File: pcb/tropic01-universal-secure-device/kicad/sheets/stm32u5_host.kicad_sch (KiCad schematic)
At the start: 1 part, among them U1 STM32U585VIT6

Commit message: feat: materialize tropic01 schematic bindings
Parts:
- U1: MountProfile Core -> (none)
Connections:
- new net: U1.10 (VSS), U1.27 (VSS), U1.49 (VSS), U1.74 (VSS), U1.99 (VSS)
- new net BOOT0: U1.62 (PD15)
- new net BTN_LEFT: U1.58 (PD11)
- new net BTN_RIGHT: U1.57 (PD10)
- new net EXP_UART_RX: U1.38 (PE7)
- new net EXP_UART_TX: U1.39 (PE8)
- new net NFC_IRQ: U1.44 (PE13)
- new net NFC_PWR_EN: U1.53 (PB14)
- new net NFC_SPI_CSN: U1.89 (PB3)
- new net NFC_SPI_MISO: U1.36 (PB1)
- new net NFC_SPI_MOSI: U1.35 (PB0)
- new net NFC_SPI_SCK: U1.37 (PB2)
- new net QSPI_CLK: U1.84 (PD3)
- new net QSPI_IO0: U1.82 (PD1)
- new net QSPI_IO1: U1.81 (PD0)
- new net QSPI_IO3: U1.46 (PE15)
- new net QSPI_NCS: U1.83 (PD2)
- new net SE2_I2C_SCL: U1.95 (PB8)
- new net SE2_I2C_SDA: U1.93 (PB7)
- new net SE2_RST: U1.96 (PB9)
- new net SWCLK: U1.16 (PC1)
- new net SWDIO: U1.17 (PC2)
- new net TFT_BACKLIGHT_PWM: U1.64 (PC7)
- new net TFT_CS: U1.67 (PA8)
- new net TFT_DC: U1.32 (PA7)
- new net TFT_PWR_EN: U1.31 (PA6)
- new net TFT_RST: U1.68 (PA9)
- new net TFT_SPI_MOSI: U1.26 (PA3)
- new net TFT_SPI_SCK: U1.30 (PA5)
- new net TOUCH_I2C_SCL: U1.92 (PB6)
- new net TOUCH_I2C_SDA: U1.91 (PB5)
- new net TOUCH_INT: U1.59 (PD12)
- new net TOUCH_RST: U1.60 (PD13)
- new net TROPIC_GPO: U1.52 (PB13)
- new net TROPIC_PWR_EN: U1.54 (PB15)
- new net TROPIC_SPI_CSN: U1.79 (PC11)
- new net TROPIC_SPI_MISO: U1.66 (PC9)
- new net TROPIC_SPI_MOSI: U1.65 (PC8)
- new net TROPIC_SPI_SCK: U1.78 (PC10)
- new net USB_DM: U1.33 (PC4)
- new net USB_DP: U1.18 (PC3)
- new net USB_VBUS_SENSE: U1.63 (PC6)
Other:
- note removed: "KiCad 10 provides MCU_ST_STM32U5:STM32U585VITx with Package_QFP:LQFP-100_14x14mm_P0.5mm; final pin assignment remains gated by pinmux review."

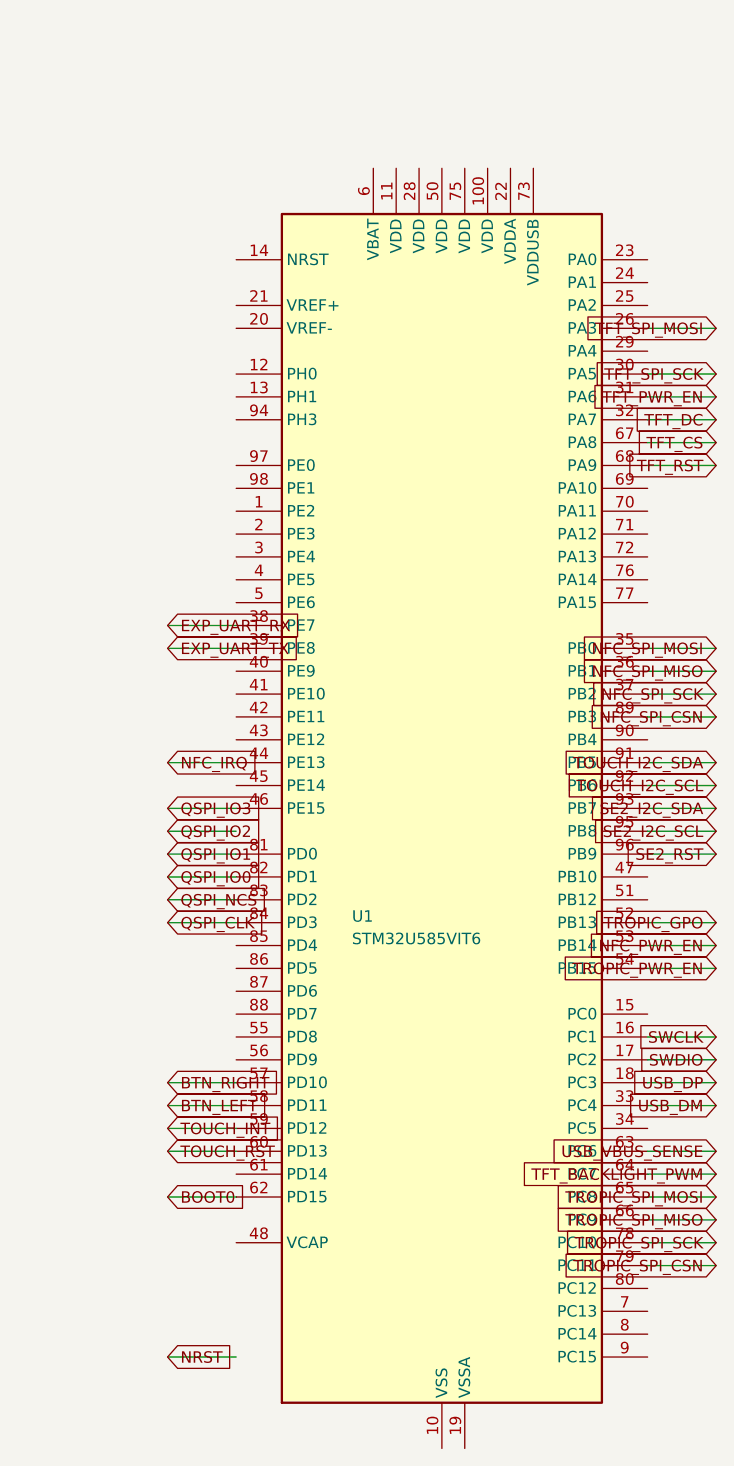
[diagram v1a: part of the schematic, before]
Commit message: feat: bind tropic01 pcb nets
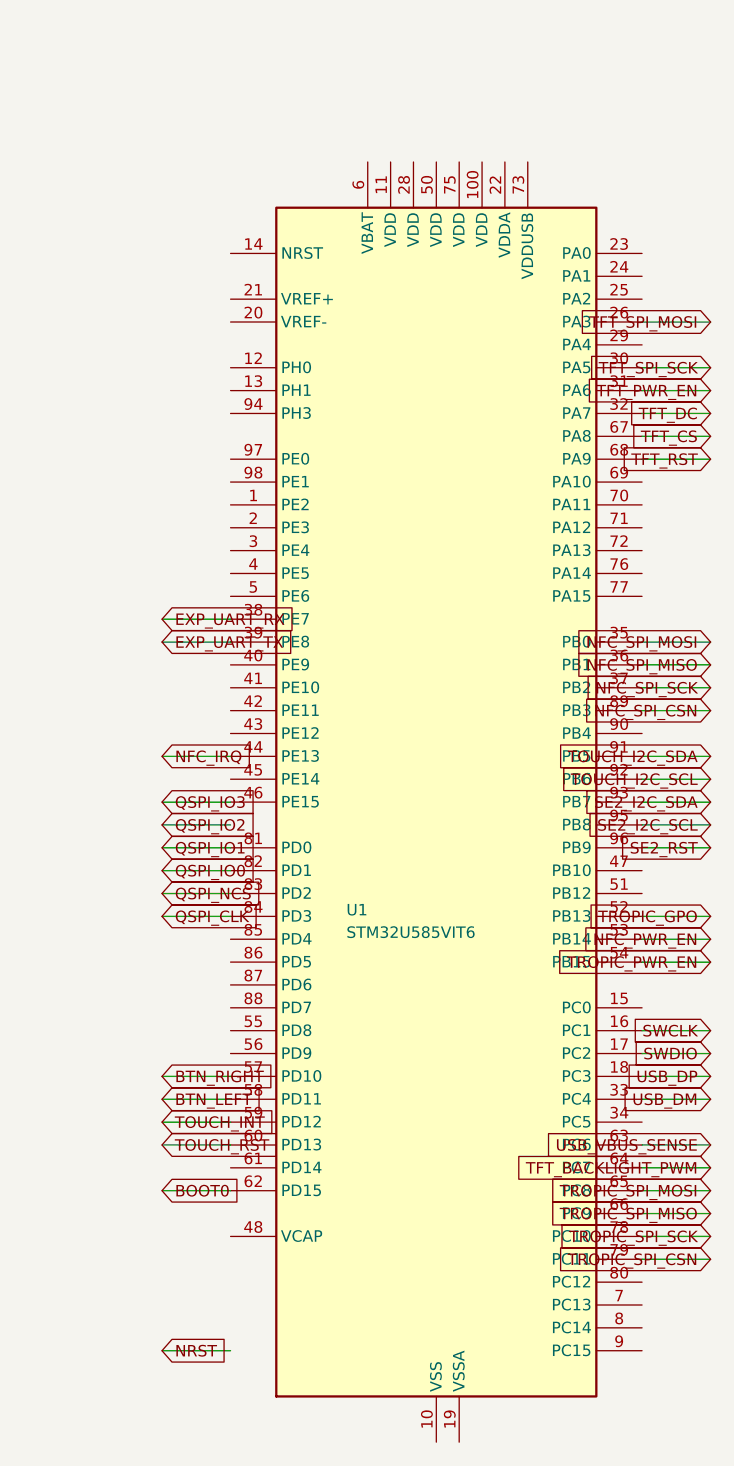
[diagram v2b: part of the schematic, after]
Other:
- moved on the sheet: U1
